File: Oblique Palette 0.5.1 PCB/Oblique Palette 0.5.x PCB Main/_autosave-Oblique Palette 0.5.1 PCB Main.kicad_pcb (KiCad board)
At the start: 2 copper layers, 235 x 110 mm, 309 parts, among them J11 Conn_01x03_Male_Pin, J13 Conn_01x03_Male_Pin, J14 Conn_01x03_Male_Pin, J16 Conn_01x03_Female_Pin, J17 AudioJack2_SwitchT, J19 Conn_01x03_Female_Pin, J2 Conn_01x03_Male_Pin, J20 AudioJack2_SwitchT, J22 Conn_01x03_Female_Pin, J23 AudioJack2_SwitchT, J25 Conn_01x03_Female_Pin, J26 AudioJack2_SwitchT, J28 Conn_01x03_Female_Pin, J29 AudioJack2_SwitchT, J31 Conn_01x03_Female_Pin, J32 AudioJack2_SwitchT, J34 Conn_01x03_Female_Pin, J35 AudioJack2_SwitchT, J37 Conn_01x03_Female_Pin, J38 AudioJack2_SwitchT, J4 Conn_01x03_Male_Pin, J40 Conn_01x03_Female_Pin, J42 AudioJack2_SwitchT, J44 Conn_01x03_Female_Pin, J46 AudioJack2_SwitchT, J48 Conn_01x03_Female_Pin, J5 Conn_01x03_Male_Pin, J50 AudioJack2_SwitchT, J52 Conn_01x03_Female_Pin, J54 AudioJack2_SwitchT, J56 Conn_01x03_Female_Pin, J58 AudioJack2_SwitchT, J60 Conn_01x03_Female_Pin, J62 AudioJack2_SwitchT, J64 Conn_01x03_Female_Pin, J66 AudioJack2_SwitchT, J68 Conn_01x03_Female_Pin, J7 Conn_01x03_Male_Pin, J70 AudioJack2_SwitchT, J72 Conn_01x02_Pin, J9 Conn_01x03_Male_Pin, U1 CD4051B, U10 MCP6004, U11 MCP4725xxx-xCH, U12 MCP6004, U13 MCP4725xxx-xCH, U14 MCP6004, U15 MCP4725xxx-xCH, U16 MCP6004, U17 MCP4725xxx-xCH, U18 MCP6004, U19 MCP4725xxx-xCH, U2 Pico, U20 MCP6004, U21 MCP4725xxx-xCH, U22 MCP6004, U23 MCP4725xxx-xCH, U24 MCP6004, U25 MCP4725xxx-xCH, U26 MCP6004, U3 MCP6004, U4 MCP6004, U5 MCP6004, U6 MCP6004, U7 MCP6004, U8 MCP6004, U9 MCP6004

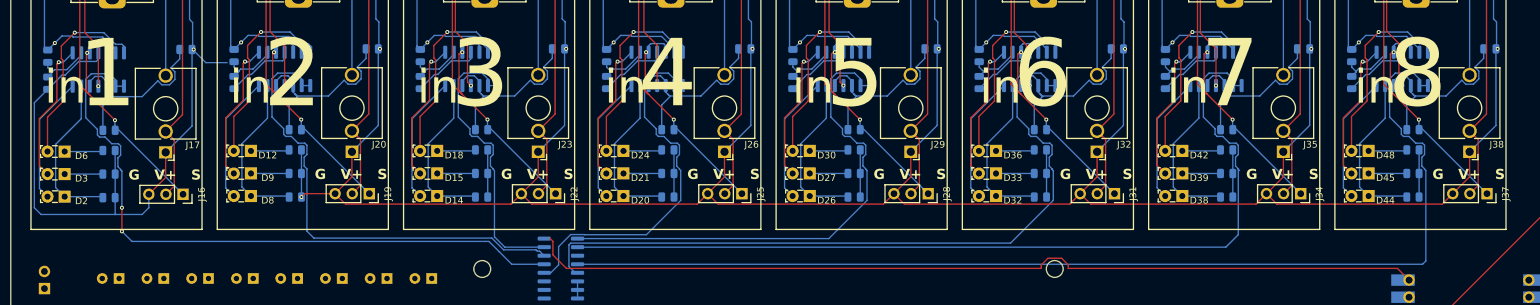
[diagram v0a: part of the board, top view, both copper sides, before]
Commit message: Input channels look to be all connected and logical now!
All inputs have their designated resistors. Channels are connected to 3v3 and GND.

Gonna beef up the power caps and turn them into SMDs.

Also gonna do up the output channels.
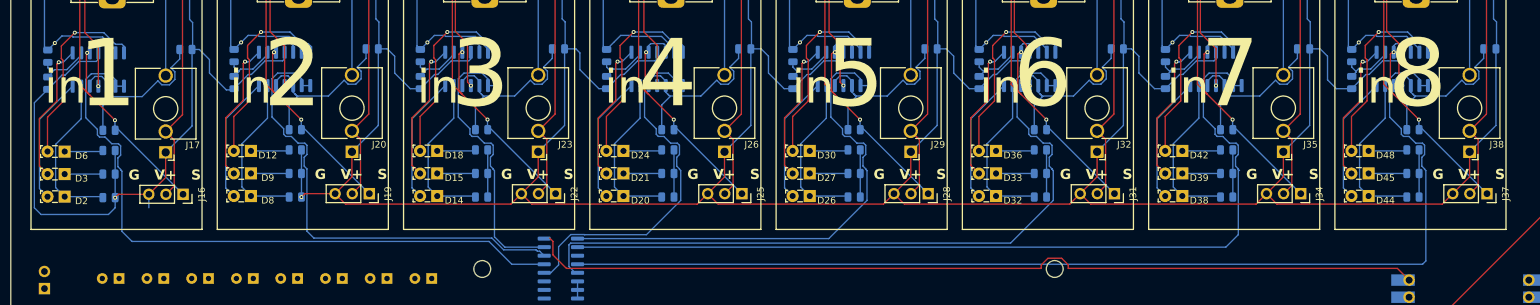
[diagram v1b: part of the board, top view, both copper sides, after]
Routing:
- net GNDREF: track 880.1 -> 945.6 mm, vias 9 -> 2
- net Net-(U6D--): vias 1 -> 0
- net /Input 1/ANALOG_CHANNEL: vias 2 -> 0
